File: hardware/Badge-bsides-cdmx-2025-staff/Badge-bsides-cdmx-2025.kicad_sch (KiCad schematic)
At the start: 30 parts, among them J1 SWDIO, J3 ADDON, J4 Conn_01x04_Pin, J5 I2C, J6 Conn_01x04_Pin, P6 USB_C_Plug_USB2.0, Q3 DMG3415U-7, SW11 ON, SW2 RESET, U1 PY32F030F28U6TR, U6 AP2112K-3.3

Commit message: feat(Hw):started_routing
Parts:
- added C67, C68, C69, C70: 10uF, Capacitor_SMD:C_0603_1608Metric, symbol Device:C_Small
- added R5, R6, R7, R8: 10k, Resistor_SMD:R_0603_1608Metric, symbol Device:R_Small
- added SW10, SW7, SW8, SW9: SW_Push, Footprints:TS1088R02026, symbol Switch:SW_Push
- J4: footprint Connector_PinHeader_2.54mm:PinHeader_1x04_P2.54mm_Vertical -> Connector_PinHeader_2.54mm:PinHeader_1x04_P2.54mm_Horizontal
- J6: footprint Connector_PinHeader_2.54mm:PinHeader_1x04_P2.54mm_Vertical -> Connector_PinSocket_2.54mm:PinSocket_1x04_P2.54mm_Horizontal
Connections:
- net +3V3: now also R5.2, R6.2, R7.2, R8.2
- net GND: now also J4.1 (Pin_1), J4.2 (Pin_2), J6.1 (Pin_1), J6.2 (Pin_2), C67.2, C68.2, C69.2, C70.2, SW10.1, SW7.1, SW8.1, SW9.1; no longer J4.3 (Pin_3), J4.4 (Pin_4), J6.3 (Pin_3), J6.4 (Pin_4)
- net GPIO1: now also J3.6 (Pin_6), U1.3 (PA7); no longer J3.5 (Pin_5), U1.17 (PA1)
- net GPIO2: now also J3.5 (Pin_5), U1.5 (PA12); no longer J3.6 (Pin_6), U1.16 (PA0)
- net LED1: now also U1.10 (PB6); no longer U1.2 (PA6)
- net LED2: now also U1.20 (PA4); no longer U1.3 (PA7)
- net RX: now also J4.3 (Pin_3), J4.4 (Pin_4); no longer J4.1 (Pin_1), J4.2 (Pin_2)
- net TX: now also J6.3 (Pin_3), J6.4 (Pin_4); no longer J6.1 (Pin_1), J6.2 (Pin_2)
- net BTTN2: now reaches U1.1 (PA5)
- net BTTN2: now also C68.1, R6.1, SW9.2
- new net BTTN1: C67.1, R5.1, SW8.2, U1.2 (PA6)
- new net BTTN3: C69.1, R7.1, SW7.2, U1.17 (PA1)
- new net BTTN4: C70.1, R8.1, SW10.2, U1.16 (PA0)
- no-connect marks 9 -> 3
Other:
- moved on the sheet: BT3, BT4

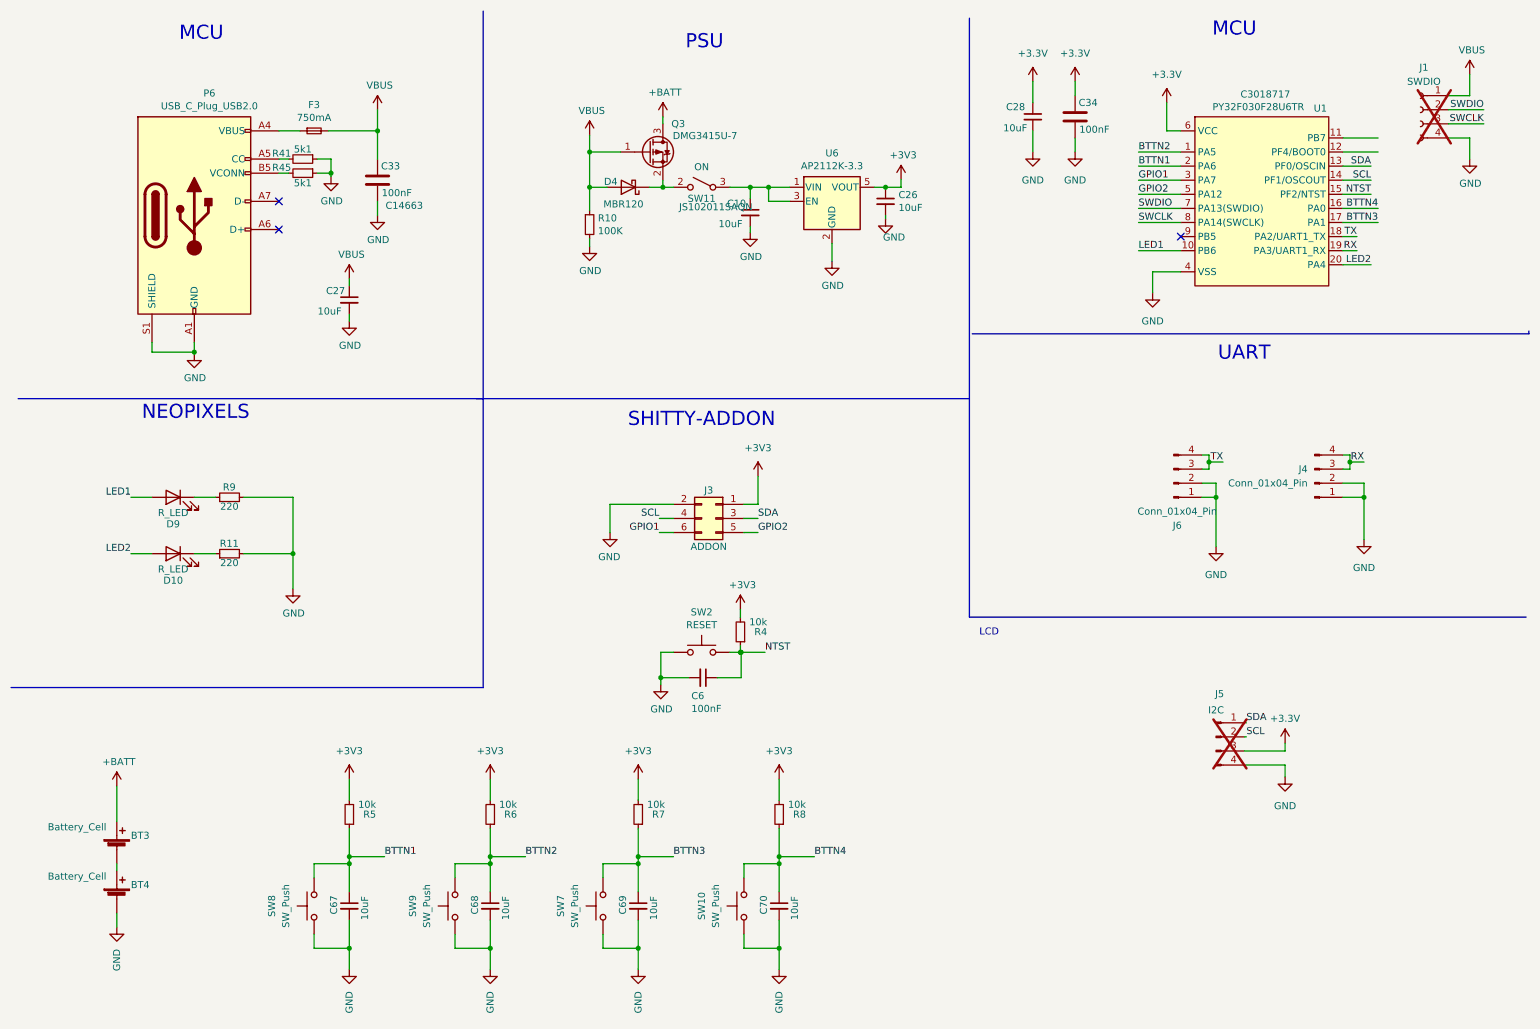
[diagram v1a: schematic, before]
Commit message: feat(Hw):Neopixels_Added_Staff
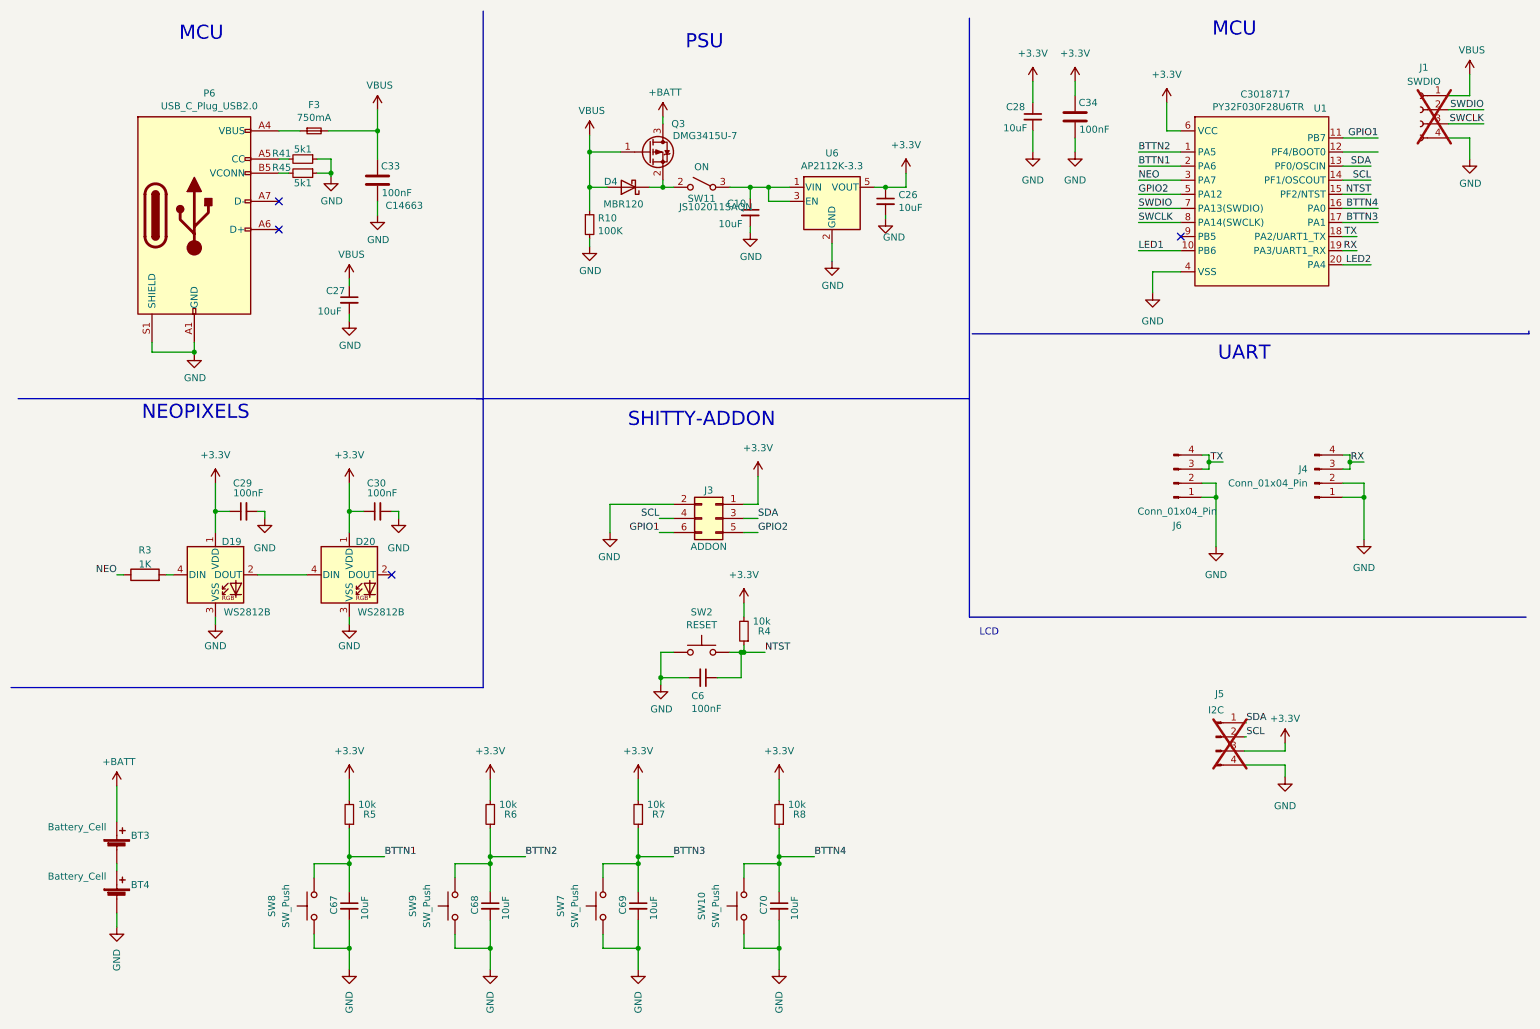
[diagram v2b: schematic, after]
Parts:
- removed D10, D9: R_LED, Footprints:LYT77K-K2M1, symbol Device:LED
- removed R11, R9: 220, Resistor_SMD:R_0603_1608Metric, symbol Device:R_Small
- added C29, C30: 100nF, Capacitor_SMD:C_0603_1608Metric, symbol Device:C_Small
- added D19, D20: WS2812B, Footprints:LED_SK6812-E, symbol LED:WS2812B
- added R3: 1K, Resistor_SMD:R_0603_1608Metric, symbol Device:R
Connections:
- net +3V3 is gone; now on net +3.3V: C26.1, J3.1 (Pin_1), R4.2, R5.2, R6.2, R7.2, R8.2, U6.5 (VOUT)
- net +3.3V: now also C29.1, C30.1, D19.1 (VDD), D20.1 (VDD)
- net +BATT: now also BT3.1 (+); no longer BT3.2 (+)
- net GND: now also C29.2, C30.2, D19.3 (VSS), D20.3 (VSS)
- net GPIO1: now also U1.11 (PB7); no longer U1.3 (PA7)
- net at BT4.2 (+): now also BT3.2 (-); no longer BT3.1 (-)
- new net: D19.4 (DIN), R3.2
- new net: D19.2 (DOUT), D20.4 (DIN)
- new net NEO: R3.1, U1.3 (PA7)
- no-connect marks 3 -> 4
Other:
- moved on the sheet: R4

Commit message: feat(HW):Staff_Updated
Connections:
- net GND: now also BT4.2 (-); no longer BT4.1 (-)
- net GPIO2: now also U1.12 (PF4/BOOT0); no longer U1.5 (PA12)
- net RX: now also J6.3 (Pin_3), J6.4 (Pin_4); no longer J4.3 (Pin_3), J4.4 (Pin_4)
- net TX: now also J4.3 (Pin_3), J4.4 (Pin_4); no longer J6.3 (Pin_3), J6.4 (Pin_4)
- net at BT3.2 (-): now also BT4.1 (+); no longer BT4.2 (+)
- net LED1: no longer names the net of U1.10 (PB6)
- net LED2: no longer names the net of U1.20 (PA4)
- no-connect marks 4 -> 7
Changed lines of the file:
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@@
+	)
+	(no_connect
+		(at 222.25 54.61)
 	)
 	(no_connect
@@
 	)
 	(no_connect
+		(at 222.25 44.45)
+	)
+	(no_connect
 		(at 59.69 50.8)
+	)
+	(no_connect
+		(at 251.46 57.15)
 	)
 	(no_connect
@@
 	(wire
 		(pts
-			(xy 214.63 44.45) (xy 222.25 44.45)
-		)
-		(stroke
-			(width 0)
-			(type default)
-		)
-	)
-	(wire
-		(pts
 			(xy 251.46 52.07) (xy 254 52.07)
 		)
@@
 	(wire
 		(pts
-			(xy 251.46 57.15) (xy 256.54 57.15)
-		)
-		(stroke
-			(width 0)
-			(type default)
-		)
-	)
-	(wire
-		(pts
 			(xy 251.46 44.45) (xy 256.54 44.45)
 		)
@@
 	(wire
 		(pts
-			(xy 214.63 54.61) (xy 222.25 54.61)
-		)
-		(stroke
-			(width 0)
-			(type default)
-		)
-	)
-	(wire
-		(pts
 			(xy 66.548 40.64) (xy 69.088 40.64)
 		)
@@
 	(wire
 		(pts
-			(xy 251.46 36.83) (xy 257.81 36.83)
-		)
-		(stroke
-			(width 0)
-			(type default)
-		)
-	)
-	(wire
-		(pts
 			(xy 48.26 101.6) (xy 50.8 101.6)
 		)
@@
 		(pts
 			(xy 91.44 177.8) (xy 91.44 180.34)
+		)
+		(stroke
+			(width 0)
+			(type default)
+		)
+	)
+	(wire
+		(pts
+			(xy 257.81 36.83) (xy 251.46 36.83)
 		)
 		(stroke
@@
 	)
 	(label "GPIO2"
-		(at 214.63 44.45 0)
-		(effects
-			(font
-				(size 1.27 1.27)
-			)
-			(justify left bottom)
+		(at 257.81 36.83 180)
+		(effects
+			(font
+				(size 1.27 1.27)
+			)
+			(justify right bottom)
 		)
 	)
@@
 	)
 	(label "TX"
-		(at 229.87 92.71 180)
-		(effects
-			(font
-				(size 1.27 1.27)
-			)
-			(justify right bottom)
+		(at 255.27 92.71 0)
+		(effects
+			(font
+				(size 1.27 1.27)
+			)
+			(justify left bottom)
 		)
 	)
@@
 		)
 	)
-	(label "LED1"
-		(at 214.63 54.61 0)
-		(effects
-			(font
-				(size 1.27 1.27)
-			)
-			(justify left bottom)
-		)
-	)
 	(label "NTST"
 		(at 256.54 44.45 180)
@@
 		)
 	)
-	(label "LED2"
-		(at 256.54 57.15 180)
-		(effects
-			(font
-				(size 1.27 1.27)
-			)
-			(justify right bottom)
-		)
-	)
 	(label "BTTN3"
 		(at 257.81 49.53 180)
@@
 	)
 	(label "RX"
-		(at 255.27 92.71 180)
-		(effects
-			(font
-				(size 1.27 1.27)
-			)
-			(justify right bottom)
-		)
-	)
+		(at 229.87 92.71 0)
+		(effects
+			(font
+				(size 1.27 1.27)
+			)
+			(justify left bottom)
+		)
+	)

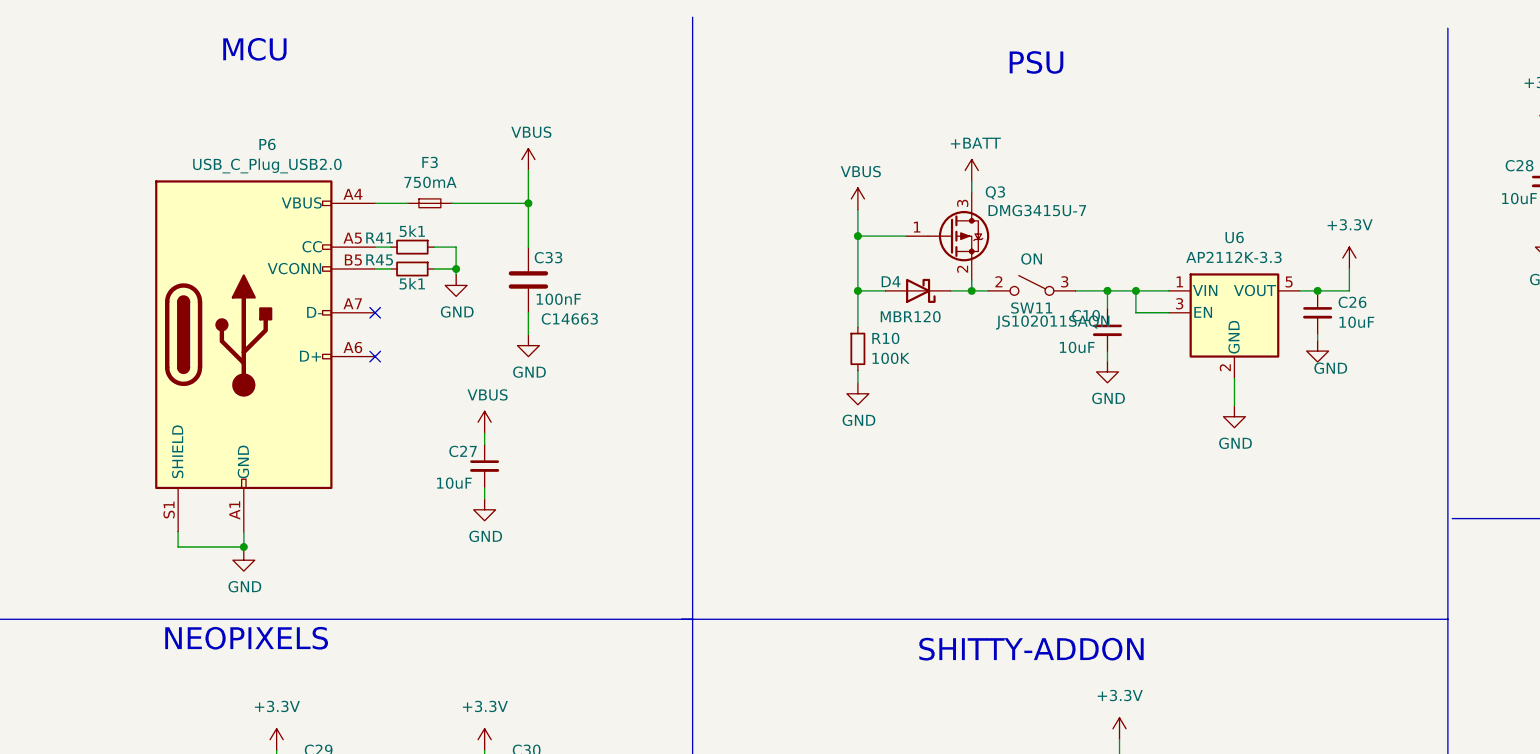
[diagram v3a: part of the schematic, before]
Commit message: feat:remove usb staff
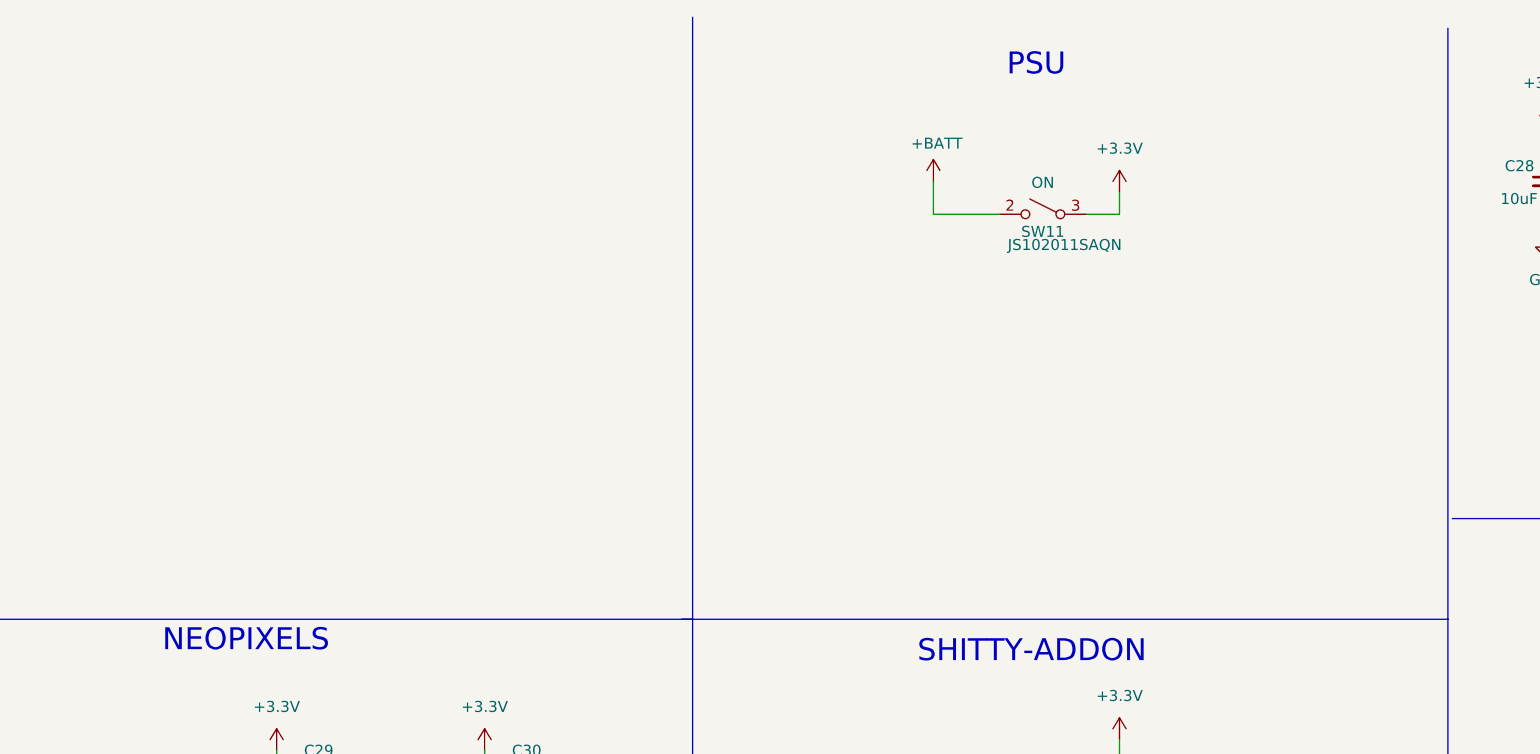
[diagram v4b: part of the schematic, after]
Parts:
- removed C10, C26, C27: 10uF, Capacitor_SMD:C_0603_1608Metric, symbol Device:C_Small
- removed C33: 100nF, Capacitor_SMD:C_0603_1608Metric, symbol Device:C
- removed D4: MBR120, Diode_SMD:D_SOD-123F, symbol Diode:MBR340
- removed F3: 750mA, Fuse:Fuse_0603_1608Metric, symbol Device:Fuse_Small
- removed P6: USB_C_Plug_USB2.0, Footprints:C393939, symbol HunterCat-NFC-rescue:USB_C_Plug_USB2.0-Connector
- removed Q3: DMG3415U-7, Package_TO_SOT_SMD:SOT-23, symbol Device:Q_PMOS_GSD
- removed R10: 100K, Resistor_SMD:R_0603_1608Metric, symbol Device:R_Small
- removed R41, R45: 5k1, Resistor_SMD:R_0603_1608Metric, symbol Device:R_Small
- removed U6: AP2112K-3.3, Package_TO_SOT_SMD:SOT-23-5, symbol HunterCat-NFC-rescue:AP2112K-3.3-Regulator_Linear
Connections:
- net +3.3V: now also SW11.3 (A)
- net +BATT: now also SW11.2 (B)
- no-connect marks 7 -> 5
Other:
- moved on the sheet: SW11

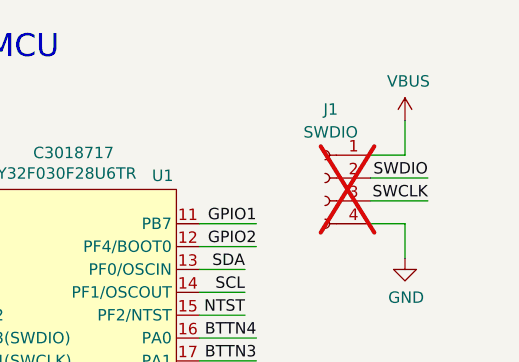
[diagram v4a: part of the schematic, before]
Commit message: fix: vbus ok staff
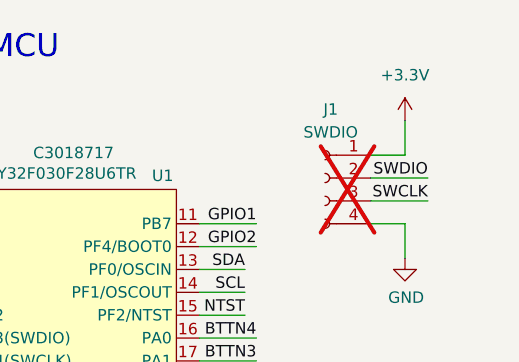
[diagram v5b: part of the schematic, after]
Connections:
- net VBUS is gone; now on net +3.3V: J1.1 (Pin_1)
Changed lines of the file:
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@@
-	)
-	(symbol
-		(lib_id "power:VBUS")
-		(at 274.32 22.86 0)
-		(unit 1)
-		(exclude_from_sim no)
-		(in_bom yes)
-		(on_board yes)
-		(dnp no)
-		(property "Reference" "#PWR032"
-			(at 274.32 26.67 0)
-			(effects
-				(font
-					(size 1.27 1.27)
-				)
-				(hide yes)
-			)
-		)
-		(property "Value" "VBUS"
-			(at 274.701 18.4658 0)
-			(effects
-				(font
-					(size 1.27 1.27)
-				)
-			)
-		)
-		(property "Footprint" ""
-			(at 274.32 22.86 0)
-			(effects
-				(font
-					(size 1.27 1.27)
-				)
-				(hide yes)
-			)
-		)
-		(property "Datasheet" ""
-			(at 274.32 22.86 0)
-			(effects
-				(font
-					(size 1.27 1.27)
-				)
-				(hide yes)
-			)
-		)
-		(property "Description" ""
-			(at 274.32 22.86 0)
-			(effects
-				(font
-					(size 1.27 1.27)
-				)
-				(hide yes)
-			)
-		)
-		(pin "1"
-		)
-		(instances
-			(project "Badge-bsides-cdmx-2025"
-				(path "/9e507f21-309f-4609-82f1-623ff0aae3c9"
-					(reference "#PWR032")
-					(unit 1)
-				)
-			)
-		)
 	)
 	(symbol
@@
 					(unit 1)
 				)
+			)
+		)
+	)
+	(symbol
+		(lib_id "power:+3.3V")
+		(at 274.32 22.86 0)
+		(unit 1)
+		(exclude_from_sim no)
+		(in_bom yes)
+		(on_board yes)
+		(dnp no)
+		(fields_autoplaced yes)
+		(property "Reference" "#PWR028"
+			(at 274.32 26.67 0)
+			(effects
+				(font
+					(size 1.27 1.27)
+				)
+				(hide yes)
+			)
+		)
+		(property "Value" "+3.3V"
+			(at 274.32 17.78 0)
+			(effects
+				(font
+					(size 1.27 1.27)
+				)
+			)
+		)
+		(property "Footprint" ""
+			(at 274.32 22.86 0)
+			(effects
+				(font
+					(size 1.27 1.27)
+				)
+				(hide yes)
+			)
+		)
+		(property "Datasheet" ""
+			(at 274.32 22.86 0)
+			(effects
+				(font
+					(size 1.27 1.27)
+				)
+				(hide yes)
+			)
+		)
+		(property "Description" "Power symbol creates a global label with name \"+3.3V\""
+			(at 274.32 22.86 0)
+			(effects
+				(font
+					(size 1.27 1.27)
+				)
+				(hide yes)
+			)
+		)
+		(pin "1"
+		)
+		(instances
+			(project "Badge-bsides-cdmx-2025"
+				(path "/9e507f21-309f-4609-82f1-623ff0aae3c9"
+					(reference "#PWR028")
+					(unit 1)
+				)
